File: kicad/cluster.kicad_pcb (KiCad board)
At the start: 2 copper layers, 24.5 x 36.5 mm, 17 parts, among them J1 Conn_01x07

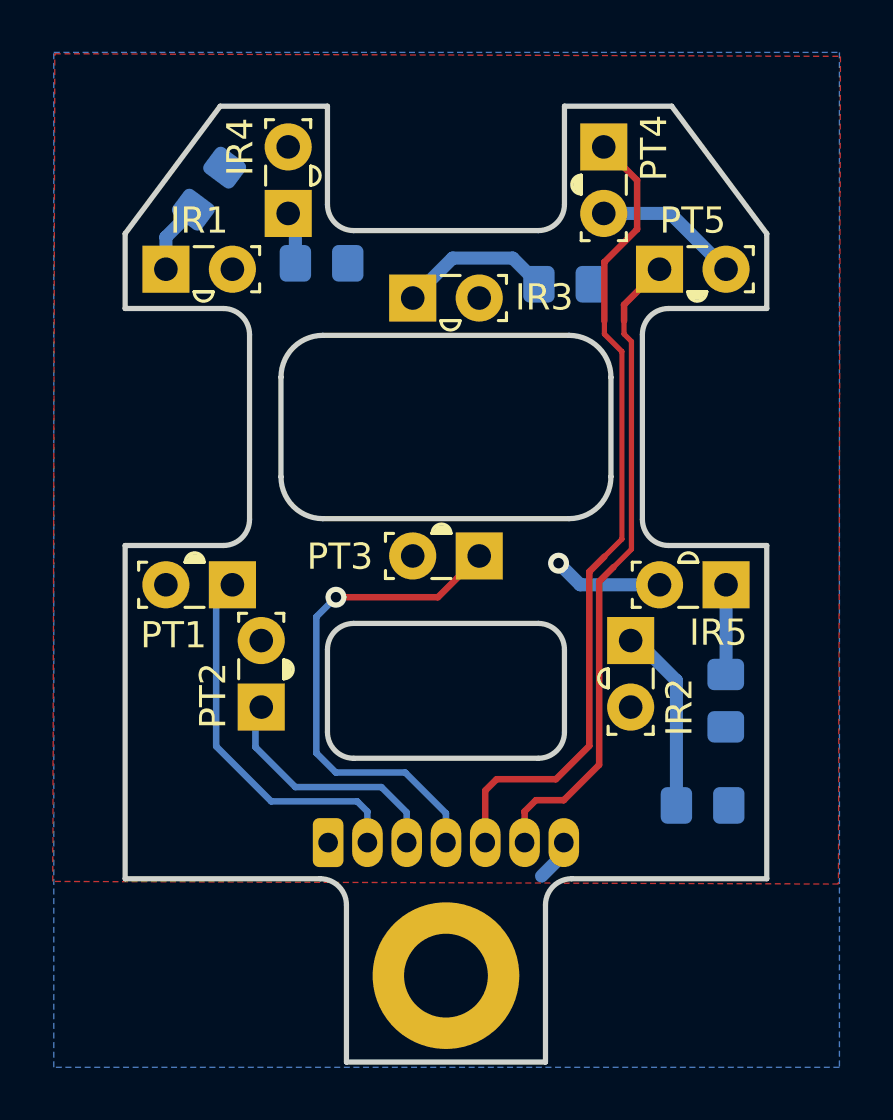
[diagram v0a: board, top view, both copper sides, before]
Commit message: Initial commit of lalboard extended features, including breakout board.
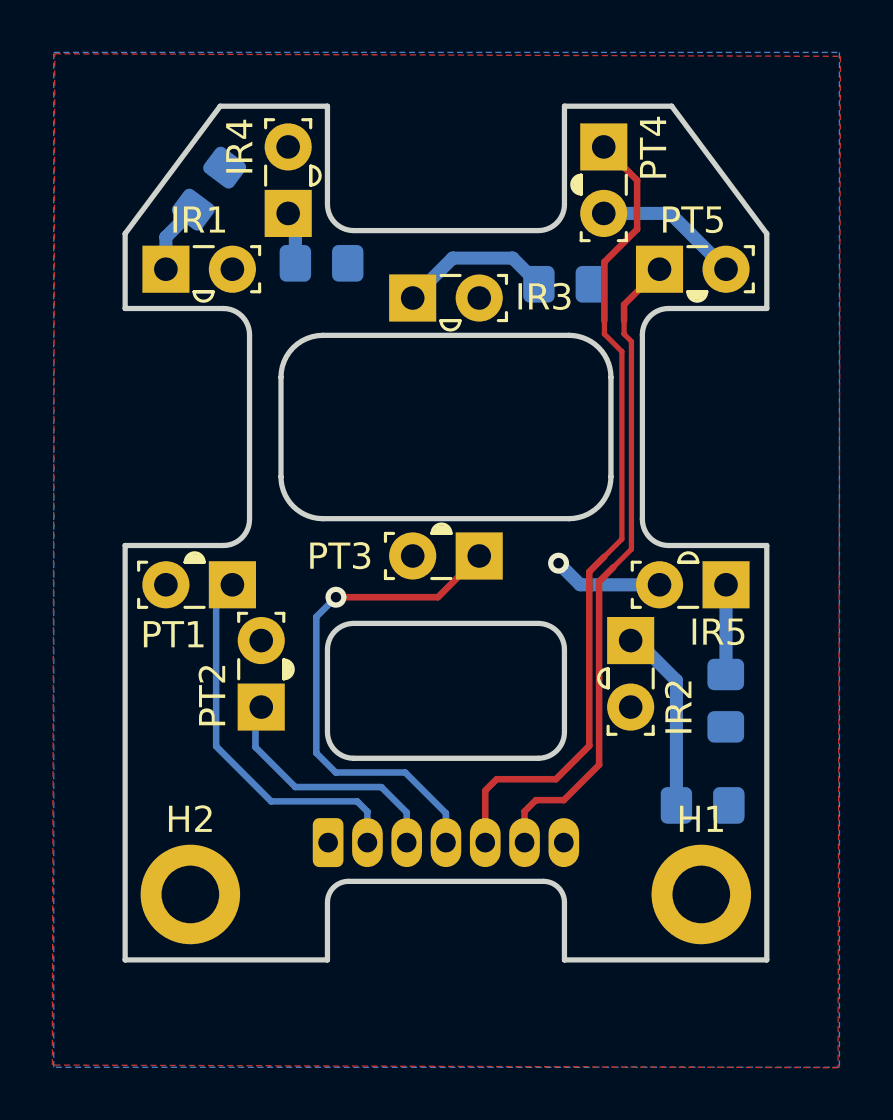
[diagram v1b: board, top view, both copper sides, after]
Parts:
- added H2: MountingHole_Pad, MountingHole:MountingHole_2.2mm_M2_DIN965_Pad, F.Cu at (152.7, 93.4)
- H1: footprint MountingHole:MountingHole_3.2mm_M3_DIN965_Pad -> MountingHole:MountingHole_2.2mm_M2_DIN965_Pad
- moved H1 10.2 mm to (172.2, 93.4)
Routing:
- net GND: track 2.31 -> 1.11 mm
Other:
- board size 24.5 x 36.5 mm -> 24.5 x 32.6 mm
